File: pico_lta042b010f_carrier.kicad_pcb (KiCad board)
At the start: 2 copper layers, 100 x 52 mm, 31 parts, among them J1 LTA042B010F_FFC_36P_0.5mm, J2 5V_INPUT, J3 CCFL_INVERTER_13V8, U1 RaspberryPi_Pico_2W, U3 MC34063AD

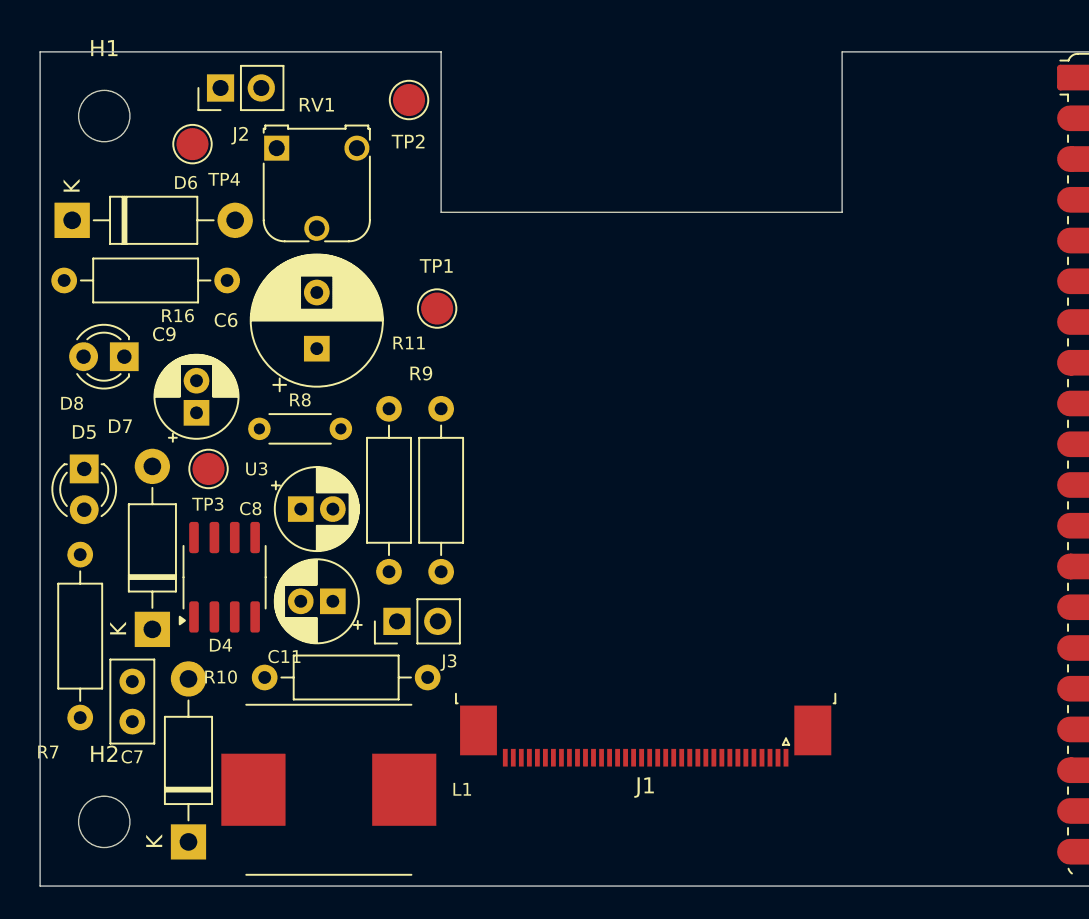
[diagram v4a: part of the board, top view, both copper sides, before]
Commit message: Update power stage for vertical parts and USB-C input
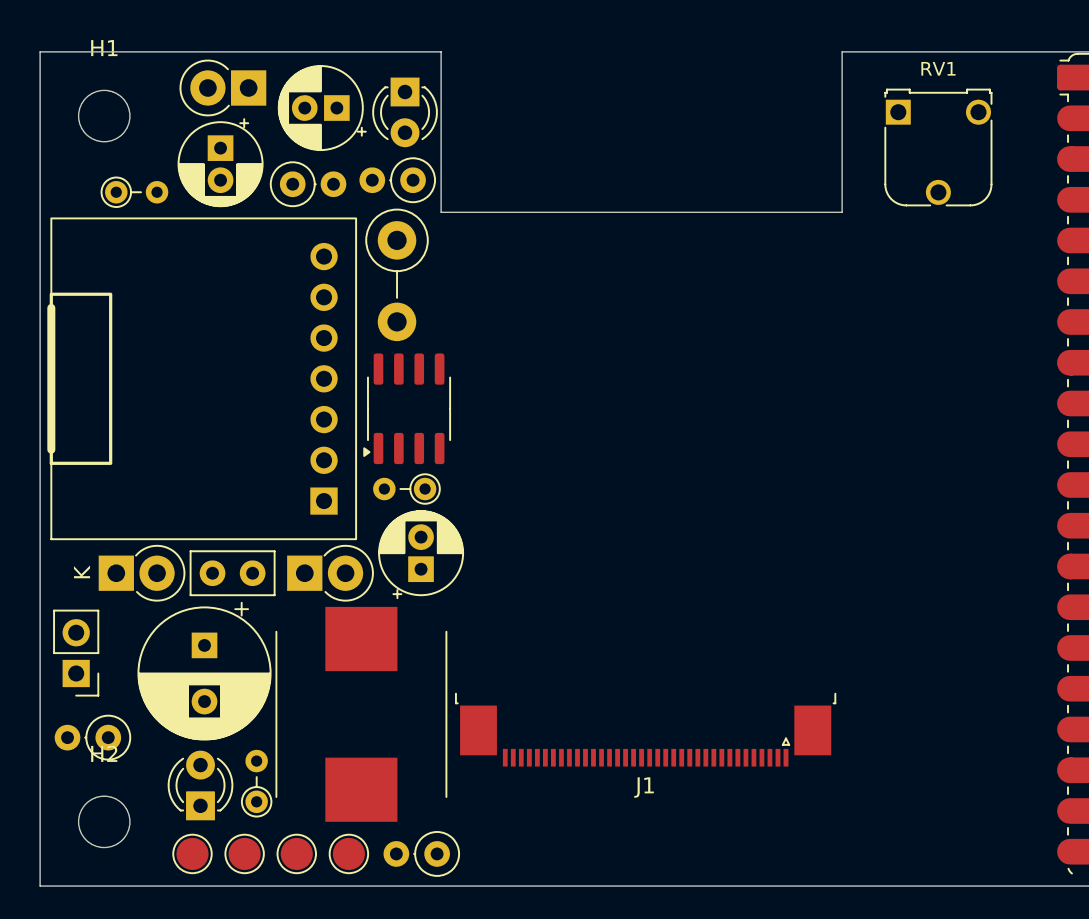
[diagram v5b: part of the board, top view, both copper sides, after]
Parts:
- added R17: 5.1k 1%, Resistor_THT:R_Axial_DIN0204_L3.6mm_D1.6mm_P2.54mm_Vertical, F.Cu at (13.5, 46.8)
- added R18: 5.1k 1%, Resistor_THT:R_Axial_DIN0204_L3.6mm_D1.6mm_P2.54mm_Vertical, F.Cu at (24.0, 27.2)
- D4, D6, D7: footprint Diode_THT:D_DO-41_SOD81_P10.16mm_Horizontal -> Diode_THT:D_DO-41_SOD81_P2.54mm_Vertical_KathodeUp
- J2: value 5V_INPUT -> USB-C 5V INPUT; footprint Connector_PinHeader_2.54mm:PinHeader_1x02_P2.54mm_Vertical -> Custom:AE_USB2.0_TYPE_C
- R10, R11, R16, R9: footprint Resistor_THT:R_Axial_DIN0207_L6.3mm_D2.5mm_P10.16mm_Horizontal -> Resistor_THT:R_Axial_DIN0207_L6.3mm_D2.5mm_P2.54mm_Vertical
- R7: footprint Resistor_THT:R_Axial_DIN0207_L6.3mm_D2.5mm_P10.16mm_Horizontal -> Resistor_THT:R_Axial_DIN0411_L9.9mm_D3.6mm_P5.08mm_Vertical
- R8: footprint Resistor_THT:R_Axial_DIN0204_L3.6mm_D1.6mm_P5.08mm_Horizontal -> Resistor_THT:R_Axial_DIN0204_L3.6mm_D1.6mm_P2.54mm_Vertical
- moved TP2 48.1 mm to (12.8, 50.0)
- moved TP4 45.3 mm to (19.2, 50.0)
- moved RV1 38.8 mm to (53.5, 3.76)
- moved TP1 37.3 mm to (9.50, 50.0)
- moved R7 35.7 mm to (22.2, 11.8), turned to -90 degrees
- moved D7 34.3 mm to (13.0, 2.25), turned to 180 degrees
- moved R10 32.4 mm to (23.2, 8.00), turned to 180 degrees
- moved D5 30.9 mm to (22.8, 2.50)
- moved C11 30.8 mm to (18.5, 3.50)
- moved R16 28.6 mm to (4.25, 42.8), turned to 180 degrees
- moved D8 28.4 mm to (10.0, 47.0), turned to 90 degrees
- moved R11 27.8 mm to (24.8, 50.0), turned to 180 degrees
- moved J2 26.5 mm to (17.7, 28.0)
- moved TP3 24.6 mm to (16.0, 50.0)
- moved D6 22.2 mm to (4.75, 32.5)
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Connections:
- J2 pad 2: GND -> (no net)

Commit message: Use compact Akizuki USB-C power connector
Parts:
- removed R17, R18: 5.1k 1%, Resistor_THT:R_Axial_DIN0204_L3.6mm_D1.6mm_P2.54mm_Vertical
- J2: footprint Custom:AE_USB2.0_TYPE_C -> Custom:A295_CTRPB_1
- moved D6 19.9 mm to (8.50, 13.0)
- moved J2 14.3 mm to (3.40, 28.0)
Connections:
- J2 pad 2: (no net) -> GND

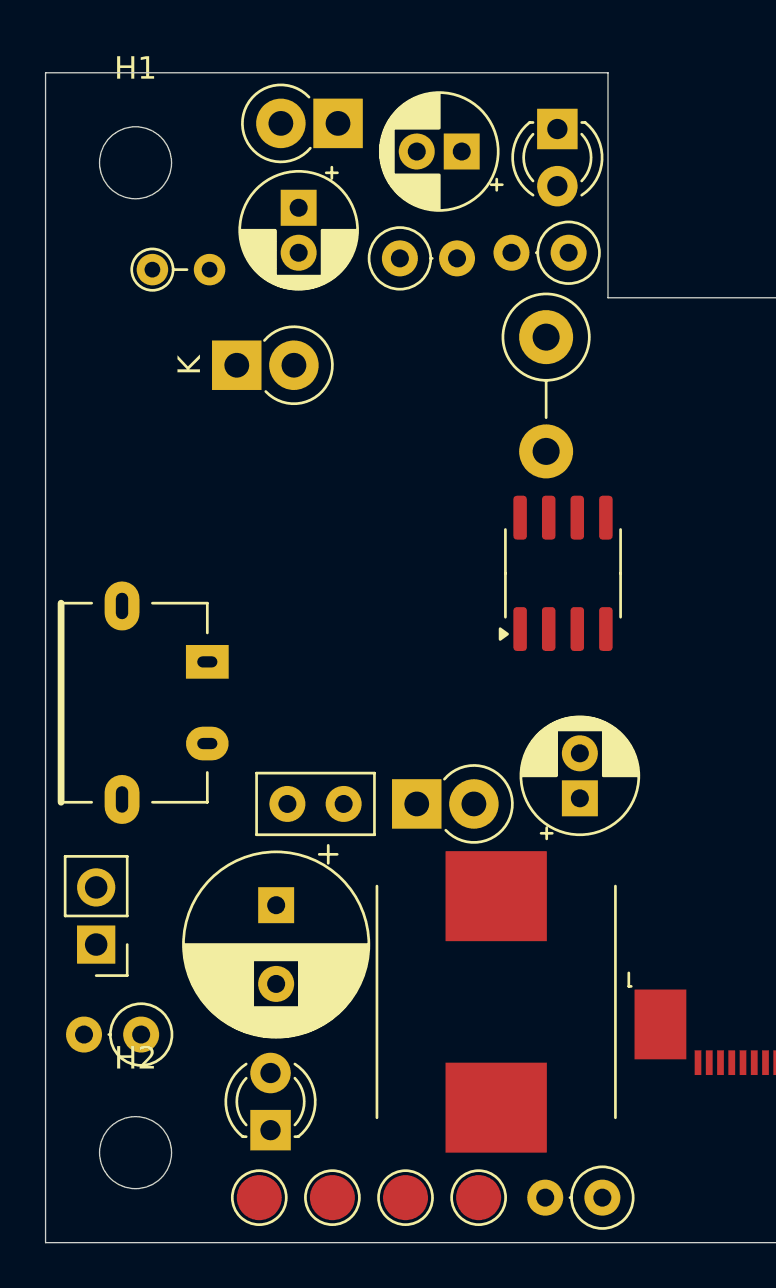
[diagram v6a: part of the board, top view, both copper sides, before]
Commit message: Optimize and route power stage
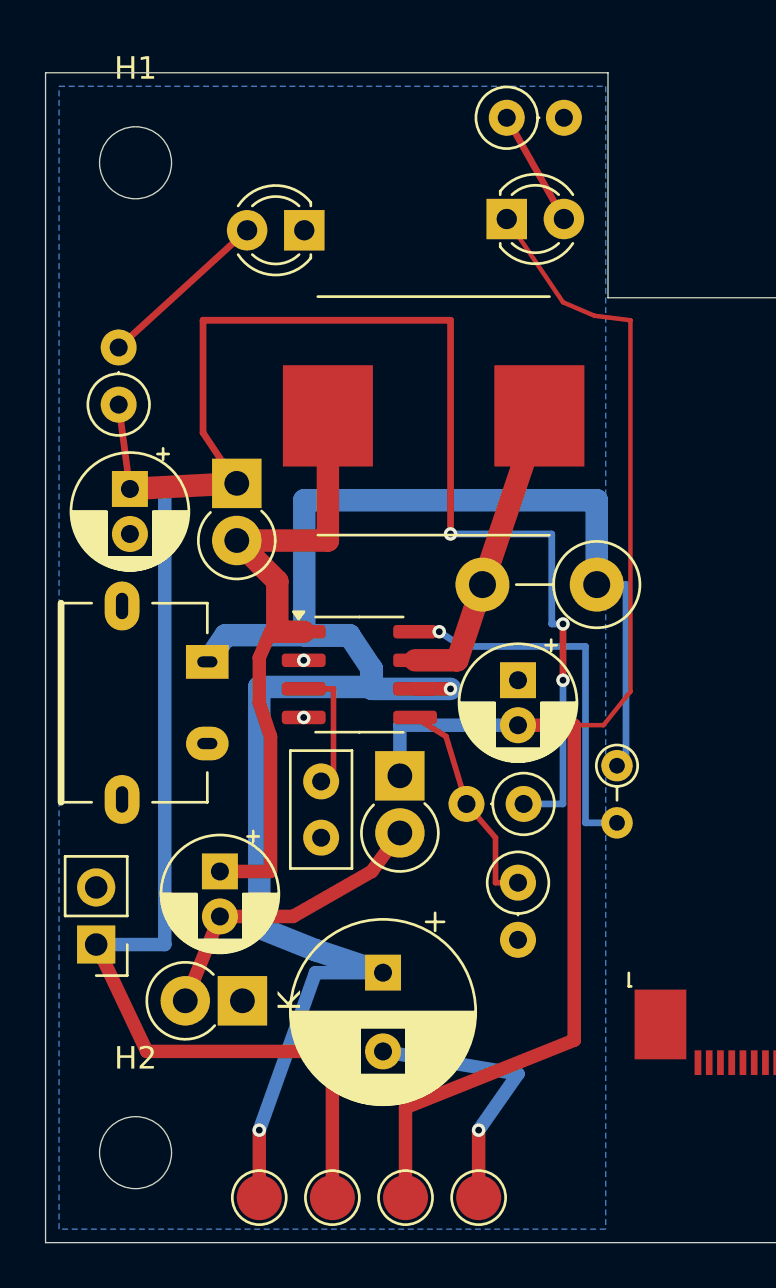
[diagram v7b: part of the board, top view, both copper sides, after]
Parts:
- moved R16 43.9 mm to (20.5, 2.00), turned to 0 degrees
- moved D8 41.8 mm to (20.5, 6.50), turned to 0 degrees
- moved R11 41.3 mm to (3.25, 14.8), turned to 90 degrees
- moved R8 30.2 mm to (25.4, 30.8), turned to -90 degrees
- moved C9 29.7 mm to (7.75, 35.5)
- moved D7 29.1 mm to (15.8, 31.2), turned to -90 degrees
- moved D6 28.3 mm to (8.75, 41.2), turned to 180 degrees
- moved R10 28.1 mm to (21.0, 36.0), turned to -90 degrees
- moved L1 26.2 mm to (17.2, 15.2), turned to 180 degrees
- moved R9 24.9 mm to (21.2, 32.5), turned to 180 degrees
- moved C8 24.3 mm to (3.75, 18.5), turned to -90 degrees
- moved C11 23.6 mm to (21.0, 27.0), turned to -90 degrees
- moved D4 16.3 mm to (8.50, 18.2), turned to -90 degrees
- moved D5 12.1 mm to (11.5, 7.00), turned to 180 degrees
- moved R7 11.2 mm to (24.5, 22.8), turned to 180 degrees
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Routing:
- net +13V8: track 0.00 -> 100.3 mm, vias 0 -> 3
- net +5V: track 0.00 -> 85.0 mm, vias 0 -> 2
- net -13V8: track 0.00 -> 65.9 mm
- net SW_NODE: track 0.00 -> 30.1 mm
- net DRIVER_DC: track 0.00 -> 17.0 mm, vias 0 -> 1
- net CPUMP_MID: track 0.00 -> 13.5 mm
- net IPK_SENSE: track 0.00 -> 13.3 mm
- net GND: track 0.00 -> 12.1 mm, vias 0 -> 3
- net VFB: track 0.00 -> 9.73 mm
- net PWR_LED_P: track 0.00 -> 7.73 mm
- net TC_TIMING: track 0.00 -> 5.99 mm
- net NEG_LED_N: track 0.00 -> 5.17 mm
- added copper zone on B.Cu, net GND

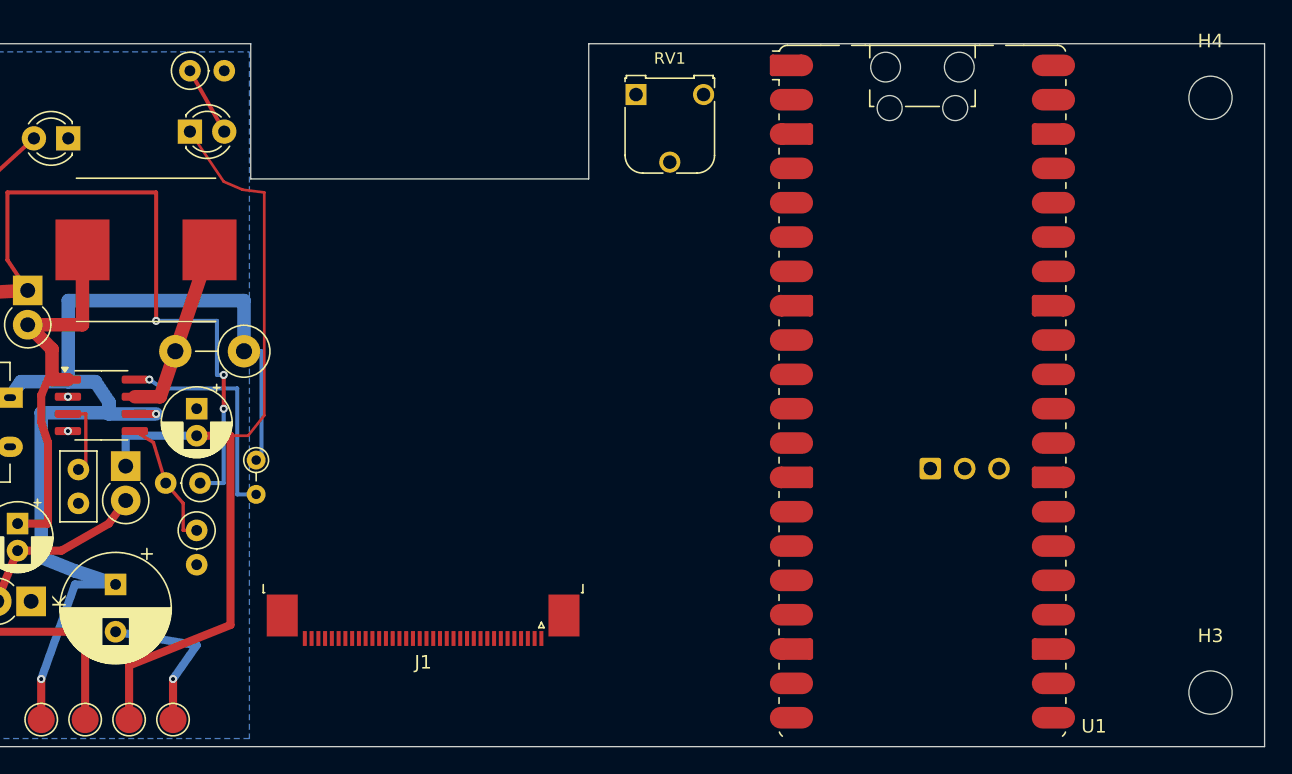
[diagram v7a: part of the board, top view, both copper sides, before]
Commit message: Route Pico and LCD connections
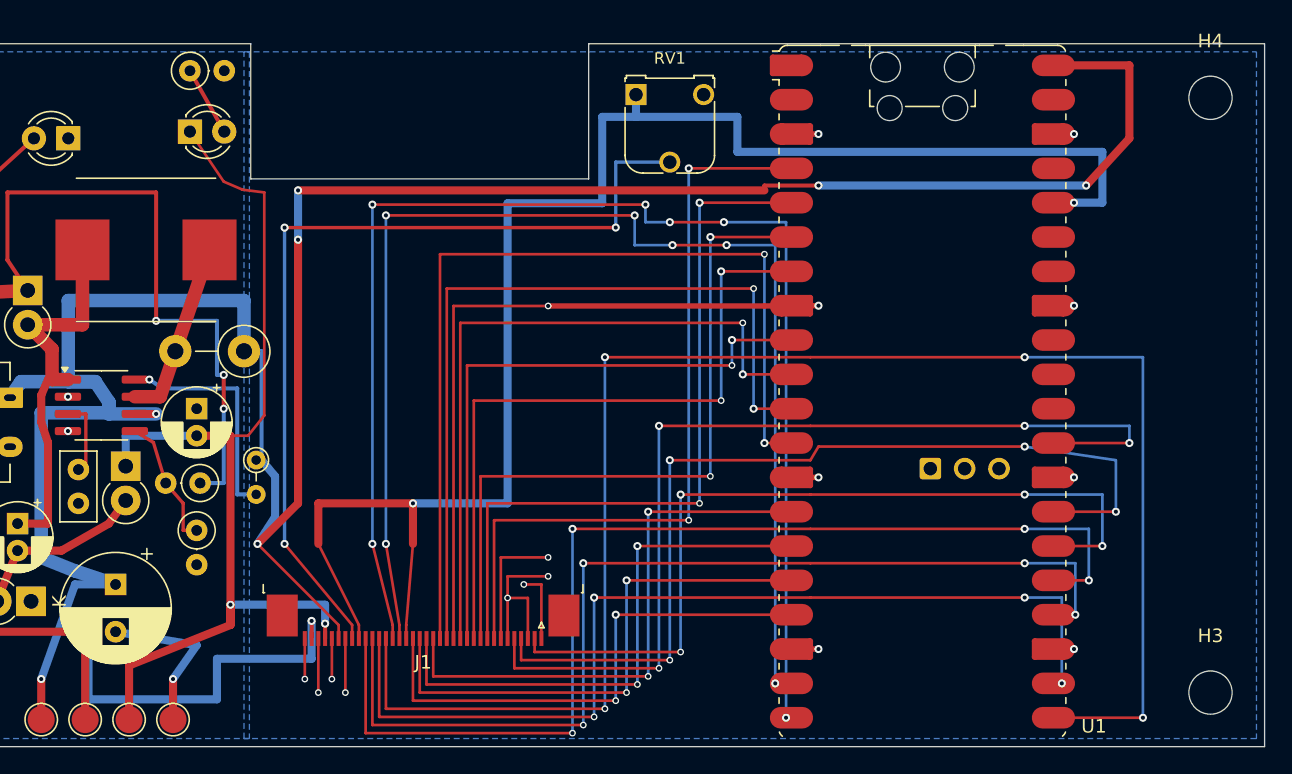
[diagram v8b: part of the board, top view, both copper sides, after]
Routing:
- net LCD_R3: track 0.00 -> 120.5 mm, vias 0 -> 4
- net +3V3: track 0.00 -> 118.9 mm, vias 0 -> 2
- net +5V: track 85.0 -> 203.2 mm, vias 2 -> 7
- net GND: track 12.1 -> 116.7 mm, vias 3 -> 20
- net LCD_R4: track 0.00 -> 101.2 mm, vias 0 -> 6
- net LCD_R5: track 0.00 -> 96.0 mm, vias 0 -> 6
- net LCD_R0: track 0.00 -> 82.0 mm, vias 0 -> 4
- net LCD_R1: track 0.00 -> 75.8 mm, vias 0 -> 4
- net LCD_VSYNC: track 0.00 -> 72.5 mm, vias 0 -> 4
- net LCD_R2: track 0.00 -> 72.1 mm, vias 0 -> 4
- net LCD_HSYNC: track 0.00 -> 69.5 mm, vias 0 -> 4
- net LCD_G4: track 0.00 -> 68.4 mm, vias 0 -> 2
- net VCPP_ADJ: track 0.00 -> 65.6 mm, vias 0 -> 3
- net LCD_NCLK: track 0.00 -> 62.1 mm, vias 0 -> 4
- net LCD_G5: track 0.00 -> 60.3 mm, vias 0 -> 2
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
